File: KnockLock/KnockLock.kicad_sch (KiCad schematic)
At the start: 39 parts, among them IC1 ESP32-C3-WROOM-02-N4, IC2 LM2575-3.3WT, IC3 MC74HC74ADTR2G, J1 2477, J2 UJ20-C-H-G-TH-P16-TR, J3 TBP04R12-500-03BE, Q1 IRLML6402TRPBF, Q2 BC547B, U1 ADXL345BCCZ-RL7

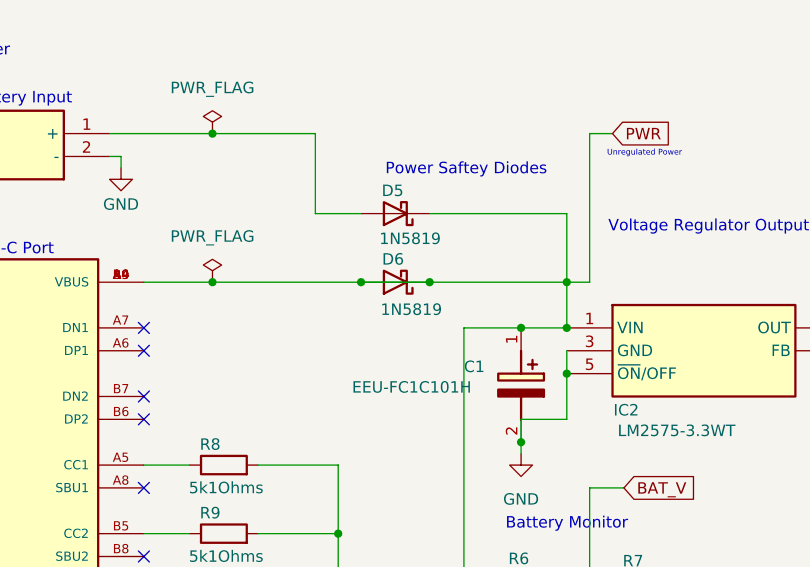
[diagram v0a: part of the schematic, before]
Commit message: Updated diode for safety margin, added diodes and servo to Partslist_Group_PE04_2.xlsx
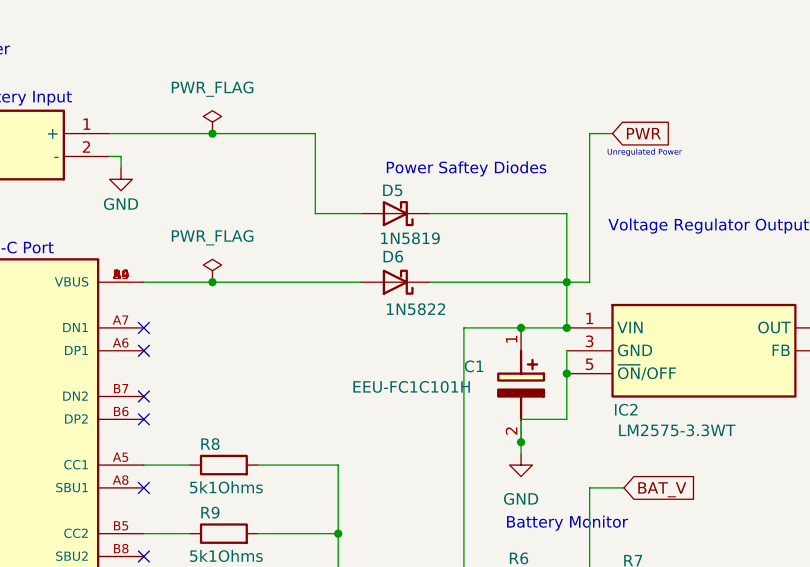
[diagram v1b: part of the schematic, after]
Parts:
- removed D6: 1N5819, Diode_THT:D_DO-41_SOD81_P10.16mm_Horizontal, symbol Diode:1N5819
- added D6: 1N5822, Diode_THT:D_DO-201AD_P15.24mm_Horizontal, symbol Diode:1N5822
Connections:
- net PWR: now also D6.1 (K); no longer J2.A4 (VBUS), J2.A9 (VBUS), J2.B4 (VBUS), J2.B9 (VBUS)
- new net: D6.2 (A), J2.A4 (VBUS), J2.A9 (VBUS), J2.B4 (VBUS), J2.B9 (VBUS)
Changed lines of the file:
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@@
 	)
 	(junction
-		(at 83.82 55.88)
-		(diameter 0)
-		(color 0 0 0 0)
-	)
-	(junction
 		(at 144.78 60.96)
 		(diameter 0)
@@
 	)
 	(junction
-		(at 76.2 55.88)
-		(diameter 0)
-		(color 0 0 0 0)
-	)
-	(junction
-		(at 59.69 55.88)
-		(diameter 0)
-		(color 0 0 0 0)
-	)
-	(junction
 		(at 99.06 66.04)
 		(diameter 0)
@@
 	)
 	(junction
+		(at 59.69 55.88)
+		(diameter 0)
+		(color 0 0 0 0)
+	)
+	(junction
 		(at 207.01 36.83)
 		(diameter 0)
@@
 	(wire
 		(pts
-			(xy 76.2 55.88) (xy 83.82 55.88)
-		)
-		(stroke
-			(width 0)
-			(type default)
-		)
-	)
-	(wire
-		(pts
 			(xy 71.12 48.26) (xy 76.2 48.26)
 		)
@@
 	(wire
 		(pts
-			(xy 59.69 55.88) (xy 76.2 55.88)
-		)
-		(stroke
-			(width 0)
-			(type default)
-		)
-	)
-	(wire
-		(pts
 			(xy 134.62 41.91) (xy 134.62 50.8)
 		)
@@
 	(wire
 		(pts
-			(xy 83.82 55.88) (xy 99.06 55.88)
-		)
-		(stroke
-			(width 0)
-			(type default)
-		)
-	)
-	(wire
-		(pts
 			(xy 175.26 130.81) (xy 212.09 130.81)
 		)
@@
 	(wire
 		(pts
+			(xy 83.82 55.88) (xy 99.06 55.88)
+		)
+		(stroke
+			(width 0)
+			(type default)
+		)
+	)
+	(wire
+		(pts
 			(xy 121.92 130.81) (xy 119.38 130.81)
 		)
@@
 	(wire
 		(pts
+			(xy 59.69 55.88) (xy 76.2 55.88)
+		)
+		(stroke
+			(width 0)
+			(type default)
+		)
+	)
+	(wire
+		(pts
 			(xy 99.06 63.5) (xy 99.06 66.04)
 		)
@@
 	)
 	(symbol
-		(lib_id "Diode:1N5819")
-		(at 80.01 55.88 180)
-		(unit 1)
-		(exclude_from_sim no)
-		(in_bom yes)
-		(on_board yes)
-		(dnp no)
-		(property "Reference" "D6"
-			(at 79.756 53.34 0)
-			(effects
-				(font
-					(size 1.27 1.27)
-				)
-			)
-		)
-		(property "Value" "1N5819"
-			(at 81.788 58.928 0)
-			(effects
-				(font
-					(size 1.27 1.27)
-				)
-			)
-		)
-		(property "Footprint" "Diode_THT:D_DO-41_SOD81_P10.16mm_Horizontal"
-			(at 80.01 51.435 0)
-			(effects
-				(font
-					(size 1.27 1.27)
-				)
-				(hide yes)
-			)
-		)
-		(property "Datasheet" "http://www.vishay.com/docs/88525/1n5817.pdf"
-			(at 80.01 55.88 0)
-			(effects
-				(font
-					(size 1.27 1.27)
-				)
-				(hide yes)
-			)
-		)
-		(property "Description" "40V 1A Schottky Barrier Rectifier Diode, DO-41"
-			(at 80.01 55.88 0)
-			(effects
-				(font
-					(size 1.27 1.27)
-				)
-				(hide yes)
-			)
-		)
-		(pin "2"
-		)
-		(pin "1"
-		)
-		(instances
-			(project ""
-				(path "/0bb14822-3a1a-451e-a409-a267c8c1fc8c"
-					(reference "D6")
-					(unit 1)
-				)
-			)
-		)
-	)
-	(symbol
 		(lib_id "Device:R")
 		(at 95.25 88.9 90)
@@
 					(unit 1)
 				)
+			)
+		)
+	)
+	(symbol
+		(lib_id "Diode:1N5822")
+		(at 80.01 55.88 180)
+		(unit 1)
+		(exclude_from_sim no)
+		(in_bom yes)
+		(on_board yes)
+		(dnp no)
+		(property "Reference" "D6"
+			(at 79.756 53.086 0)
+			(effects
+				(font
+					(size 1.27 1.27)
+				)
+			)
+		)
+		(property "Value" "1N5822"
+			(at 82.296 58.928 0)
+			(effects
+				(font
+					(size 1.27 1.27)
+				)
+			)
+		)
+		(property "Footprint" "Diode_THT:D_DO-201AD_P15.24mm_Horizontal"
+			(at 80.01 51.435 0)
+			(effects
+				(font
+					(size 1.27 1.27)
+				)
+				(hide yes)
+			)
+		)
+		(property "Datasheet" "http://www.vishay.com/docs/88526/1n5820.pdf"
+			(at 80.01 55.88 0)
+			(effects
+				(font
+					(size 1.27 1.27)
+				)
+				(hide yes)
+			)
+		)
+		(property "Description" "40V 3A Schottky Barrier Rectifier Diode, DO-201AD"
+			(at 80.01 55.88 0)
+			(effects
+				(font
+					(size 1.27 1.27)
+				)
+				(hide yes)
+			)
+		)
+		(pin "2"
+		)
+		(pin "1"
+		)
+		(instances
+			(project ""
+				(path "/0bb14822-3a1a-451e-a409-a267c8c1fc8c"
+					(reference "D6")
+					(unit 1)
+				)

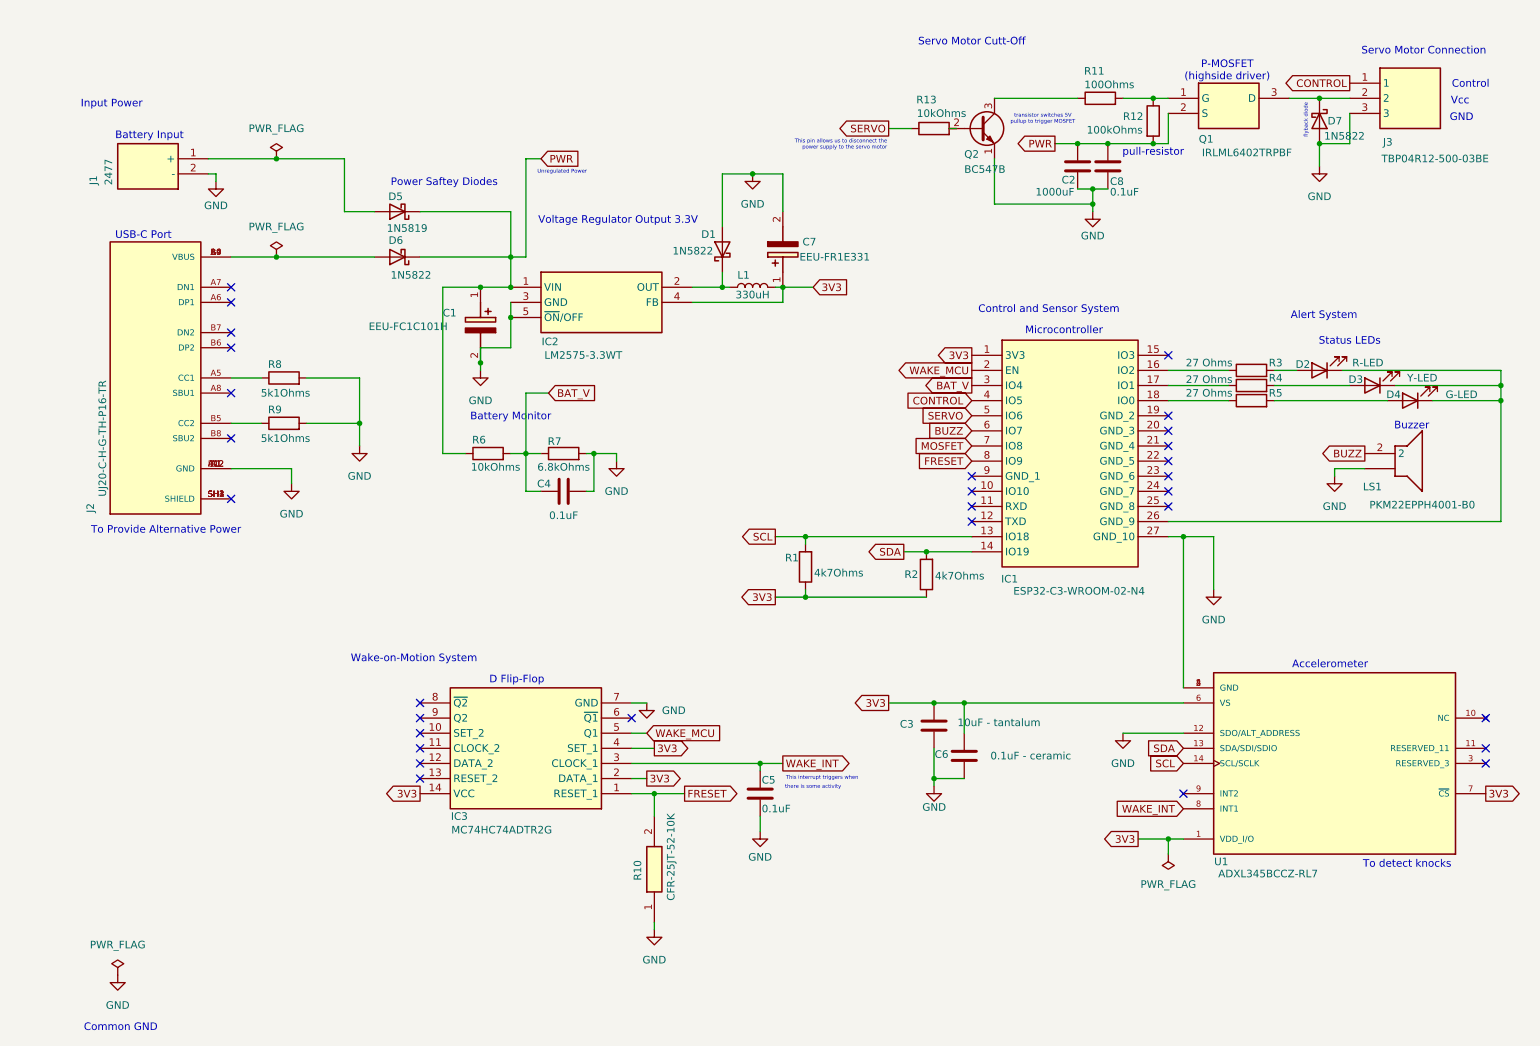
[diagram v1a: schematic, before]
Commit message: Some pcb refinement
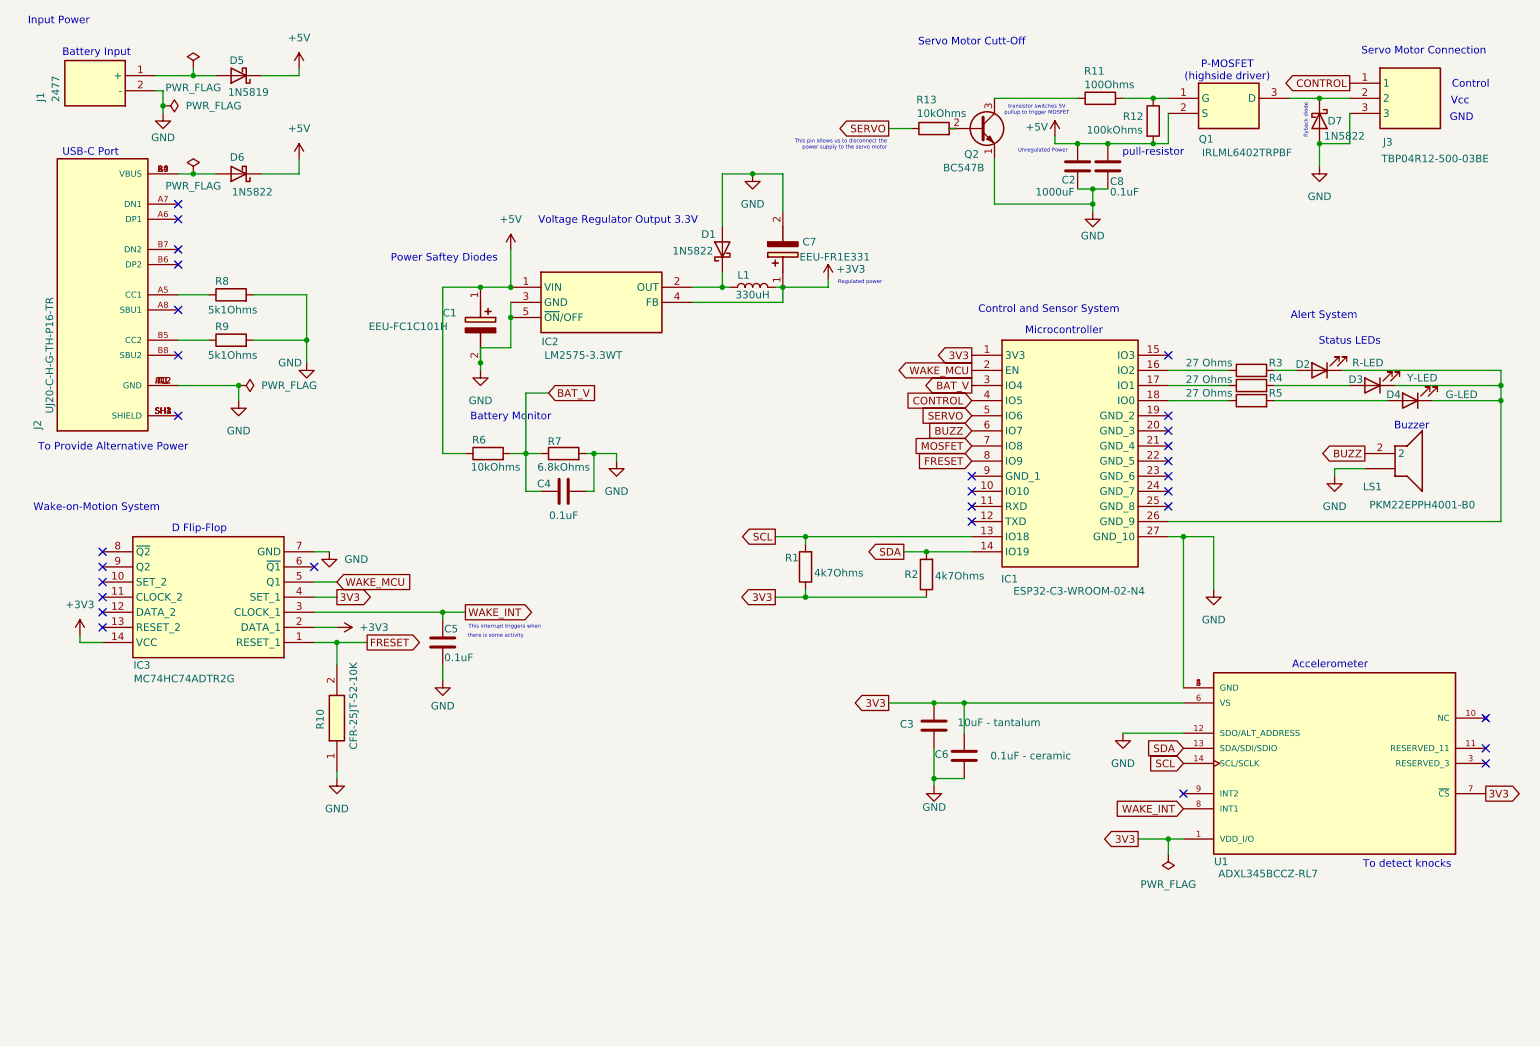
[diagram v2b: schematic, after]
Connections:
- net 3V3: no longer C7.1 (+), IC2.4 (FB), IC3.14 (VCC), IC3.2 (DATA_1), L1.2
- net PWR renamed +5V
- new net +3V3: C7.1 (+), IC2.4 (FB), IC3.14 (VCC), IC3.2 (DATA_1), L1.2
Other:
- note added: "Regulated power"
- note removed: "Common GND"
- moved on the sheet: C5, D5, D6, IC3, J1, J2, R10, R8, R9
